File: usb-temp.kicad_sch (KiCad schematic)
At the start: 11 parts, among them J1 Conn_01x02_Pin, J2 USB_MB, J3 Conn_01x05, U1 STM32F042F4Px, U2 ZLDO1117G33TA

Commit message: First Order
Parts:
- removed J1: Conn_01x02_Pin, Connector_PinHeader_2.54mm:PinHeader_1x02_P2.54mm_Vertical, symbol Connector:Conn_01x02_Pin
- removed R1: R-10k-0603, Resistor_SMD:R_0603_1608Metric_Pad0.98x0.95mm_HandSolder, symbol MyLib:R-10k-1206-0.1%
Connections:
- net +5V: now also J2.2 (VBUS); no longer J2.1 (VBUS)
- net GND: now also J2.8 (GND); no longer J2.7 (GND)
- net USB_D+: now also J2.6 (D+); no longer J2.5 (D+)
- net USB_D-: now also J2.4 (D-); no longer J2.3 (D-)
- net A_Input0/A: now reaches U1.6 (PA0)
- net at USB_2_Out1.1 (Pin_1): now also J2.1 (VBUS); no longer J2.2 (VBUS)
- net at USB_2_Out1.2 (Pin_2): now also J2.3 (D-); no longer J2.4 (D-)
- net at USB_2_Out1.3 (Pin_3): now also J2.5 (D+); no longer J2.6 (D+)
- net at USB_2_Out1.4 (Pin_4): now also J2.7 (GND); no longer J2.8 (GND)
- net A_Input6/A: now reaches U1.10 (PA4)
- net A_Input5/A: now reaches U1.11 (PA5)
- net A_Input4/A: now reaches U1.12 (PA6)
- net A_Input7/A: now reaches U1.13 (PA7)
- net A_Input1/A: now reaches U1.7 (PA1)
- net A_Input2/A: now reaches U1.8 (PA2)
- net A_Input3/A: now reaches U1.9 (PA3)
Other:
- added sheet A_Input0 (analog_input.kicad_sch)
- added sheet A_Input1 (analog_input.kicad_sch)
- added sheet A_Input2 (analog_input.kicad_sch)
- added sheet A_Input3 (analog_input.kicad_sch)
- added sheet A_Input4 (analog_input.kicad_sch)
- added sheet A_Input5 (analog_input.kicad_sch)
- added sheet A_Input6 (analog_input.kicad_sch)
- added sheet A_Input7 (analog_input.kicad_sch)

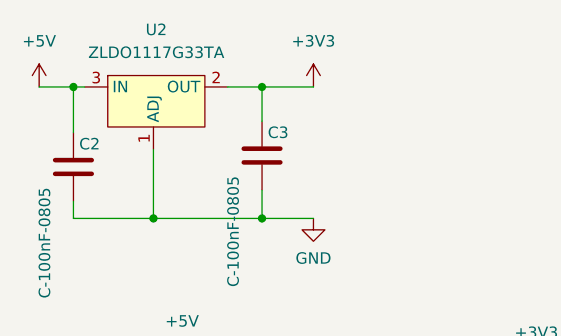
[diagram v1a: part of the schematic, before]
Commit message: new stab, as old is deprecated
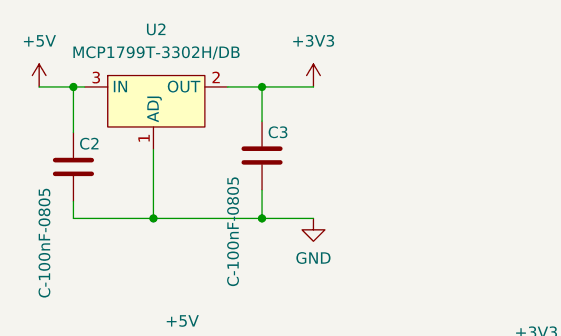
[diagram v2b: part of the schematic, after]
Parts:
- U2: value ZLDO1117G33TA -> MCP1799T-3302H/DB
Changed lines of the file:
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@@
       (effects (font (size 1.27 1.27)))
     )
-    (property "Value" "ZLDO1117G33TA" (at 31.4325 19.05 0)
+    (property "Value" "MCP1799T-3302H/DB" (at 31.4325 19.05 0)
       (effects (font (size 1.27 1.27)))
     )
@@
       (effects (font (size 1.27 1.27)) hide)
     )
-    (property "Datasheet" "https://www.reichelt.at/at/en/ldo-voltage-regulator-3-3v-sot-223-3-zldo1117g33ta-p219149.html?&trstct=pos_13&nbc=1" (at 31.115 20.32 0)
+    (property "Datasheet" "https://www.mouser.at/ProductDetail/Microchip-Technology/MCP1799T-3302H-DB?qs=BJlw7L4Cy7%2F9AvPRs1acXA%3D%3D" (at 31.115 20.32 0)
       (effects (font (size 1.27 1.27)) hide)
     )

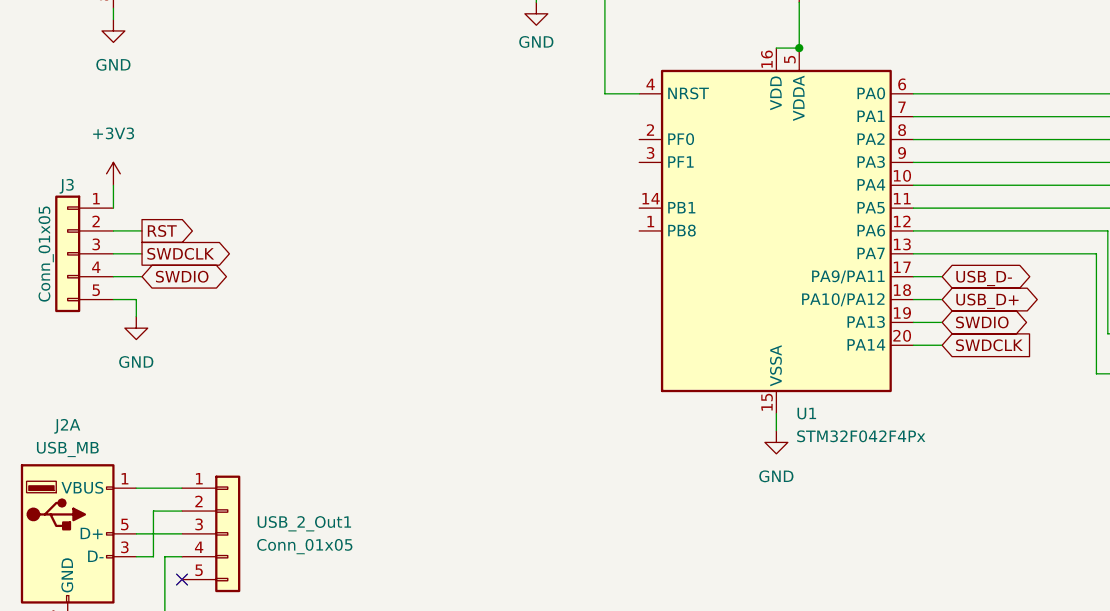
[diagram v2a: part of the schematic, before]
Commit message: Switching to new desing, small swd
working on v2.0
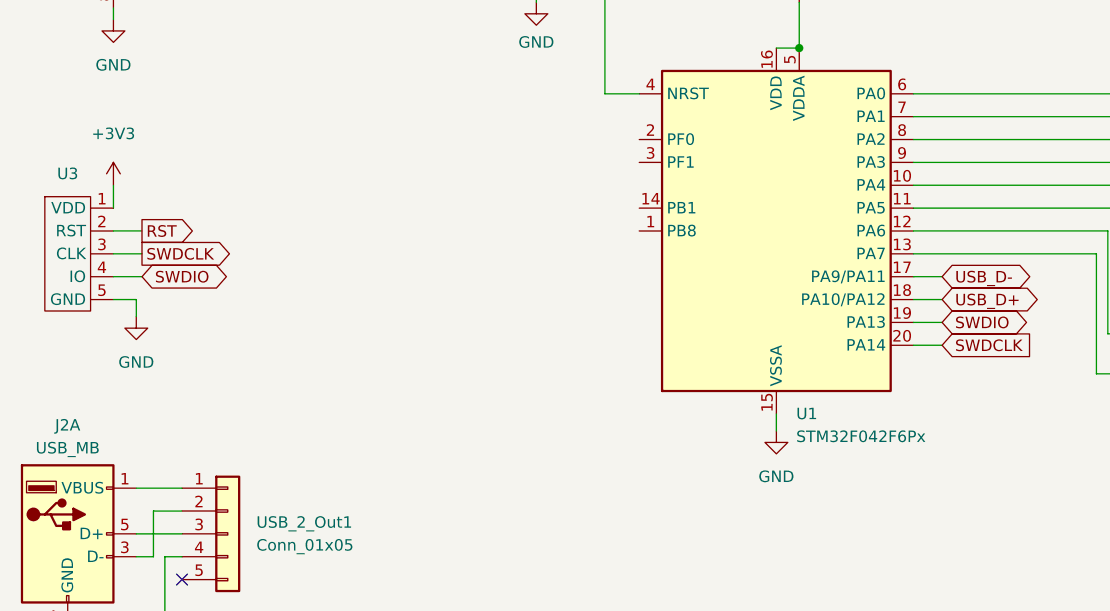
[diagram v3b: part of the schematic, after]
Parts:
- removed J3: Conn_01x05, Connector_PinHeader_2.54mm:PinHeader_1x05_P2.54mm_Vertical, symbol Connector_Generic:Conn_01x05
- added U3: ~, eurorack:1.27 SWD Programmer, symbol eurorack:SWD
- U1: value STM32F042F4Px -> STM32F042F6Px
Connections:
- net +3V3: now also U3.1 (VDD)
- net GND: now also U3.5 (GND)
- net RST: now also U3.2 (RST)
- net SWDCLK: now also U3.3 (CLK)
- net SWDIO: now also U3.4 (IO)
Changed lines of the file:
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@@
+    )
+  )
+  (symbol (lib_id "eurorack:SWD") (at 24.13 95.25 0) (unit 1)
+    (in_bom yes) (on_board yes) (dnp no) (fields_autoplaced)
+    (property "Reference" "U3" (at 21.59 93.98 0)
+      (effects (font (size 1.27 1.27)))
+    )
+    (property "Value" "~" (at 24.13 95.25 0)
+      (effects (font (size 1.27 1.27)))
+    )
+    (property "Footprint" "eurorack:1.27 SWD Programmer" (at 24.13 95.25 0)
+      (effects (font (size 1.27 1.27)) hide)
+    )
+    (property "Datasheet" "" (at 24.13 95.25 0)
+      (effects (font (size 1.27 1.27)) hide)
+    )
+    (pin "2")
+    (pin "1")
+    (pin "5")
+    (pin "3")
+    (pin "4")
+    (instances
+      (project "usb-temp"
+        (path "/c76a25ea-17ab-4d1a-b59e-ff5ac2c98874"
+          (reference "U3") (unit 1)
+        )
+      )
     )
   )
@@
       (effects (font (size 1.27 1.27)) (justify left))
     )
-    (property "Value" "STM32F042F4Px" (at 102.5241 123.19 0)
+    (property "Value" "STM32F042F6Px" (at 102.5241 123.19 0)
       (effects (font (size 1.27 1.27)) (justify left))
     )
@@
         )
       )
-    )
-  )
-  (symbol (lib_id "Connector_Generic:Conn_01x05") (at 21.59 102.87 0) (mirror y) (unit 1)
-    (in_bom yes) (on_board yes) (dnp no)
-    (property "Reference" "J3" (at 21.59 95.25 0)
-      (effects (font (size 1.27 1.27)))
-    )
-    (property "Value" "Conn_01x05" (at 19.05 102.87 90)
-      (effects (font (size 1.27 1.27)))
-    )
-    (property "Footprint" "Connector_PinHeader_2.54mm:PinHeader_1x05_P2.54mm_Vertical" (at 21.59 102.87 0)
-      (effects (font (size 1.27 1.27)) hide)
-    )
-    (property "Datasheet" "~" (at 21.59 102.87 0)
-      (effects (font (size 1.27 1.27)) hide)
-    )
-    (pin "1")
-    (pin "2")
-    (pin "3")
-    (pin "4")
-    (pin "5")
-    (instances
-      (project "usb-temp"
-        (path "/c76a25ea-17ab-4d1a-b59e-ff5ac2c98874"
-          (reference "J3") (unit 1)
-        )
-      )
